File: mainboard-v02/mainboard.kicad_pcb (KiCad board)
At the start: 4 copper layers, 90.2 x 95.9 mm, 137 parts, among them J1 503182-1852, J2 Conn_01x05, J3 10118194-0001LF, J4 DCJ0303, J5 Conn_Coaxial, J6 Conn_Coaxial, J7 Conn_Coaxial, J8 Conn_01x03, Q1 IRLML2803, Q2 2N5088, Q3 2N5088, Q4 IRLML2803, Q5 IRLML2803, Q6 IRLML2803, Q7 IRLML2803, Q8 IRLML2803, SW1 KMR231NG LFS, U1 MAX708RESA-T, U10 XTB-40, U11 XTB-40, U12 XTB-40, U13 EP2W+, U14 S1216V8, U15 RFM23BP, U16 PE014006, U17 PE014006, U18 NDS8434, U19 NDS8434, U2 ATSAMD51J20A-AU, U20 NDS8434, U21 NDS8434, U22 NDS8434, U3 LSM9DS1, U4 MAX4372TEUK+T, U5 TPS54226PWPRPWP14_2P31X2P46-L, U6 LTC4121, U7 NDS8434, U8 MR25H40MDF, U9 XTB-40, Y1 32.768kHz

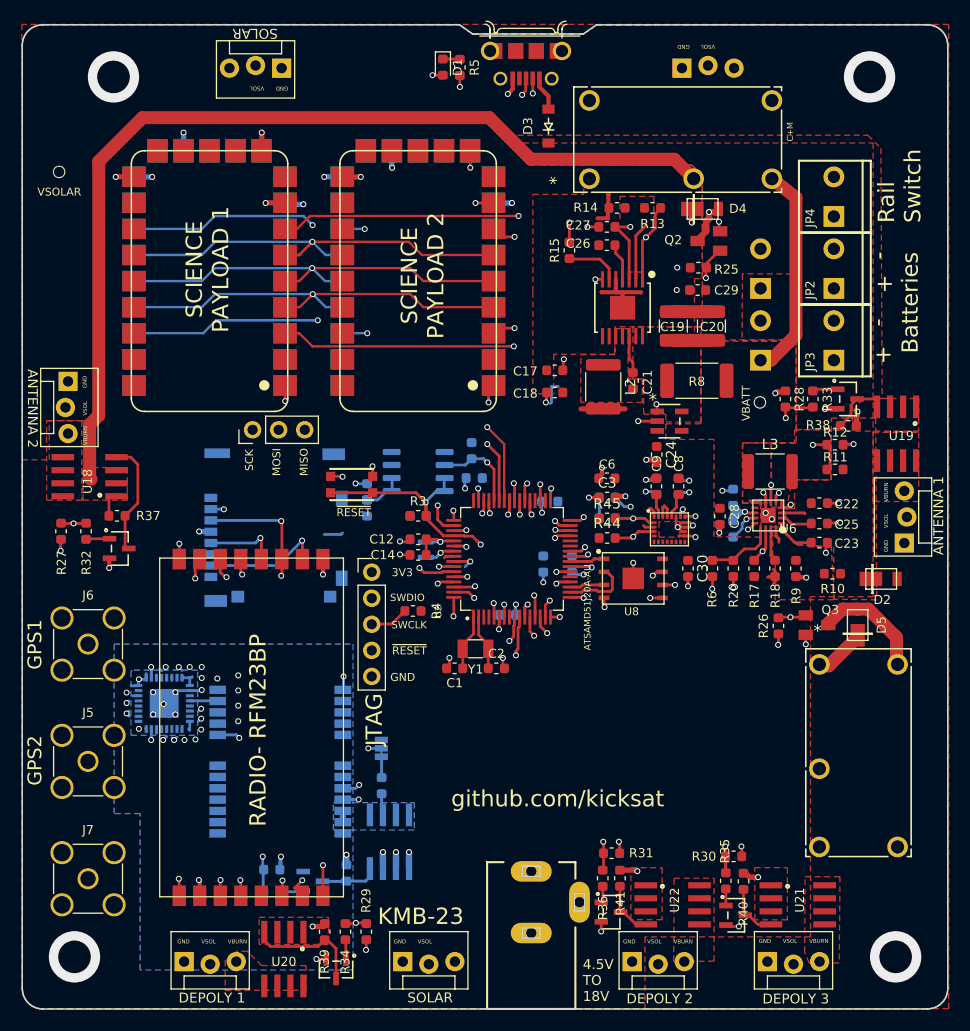
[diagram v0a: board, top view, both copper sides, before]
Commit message: mainboard-v02 with RFM98PW
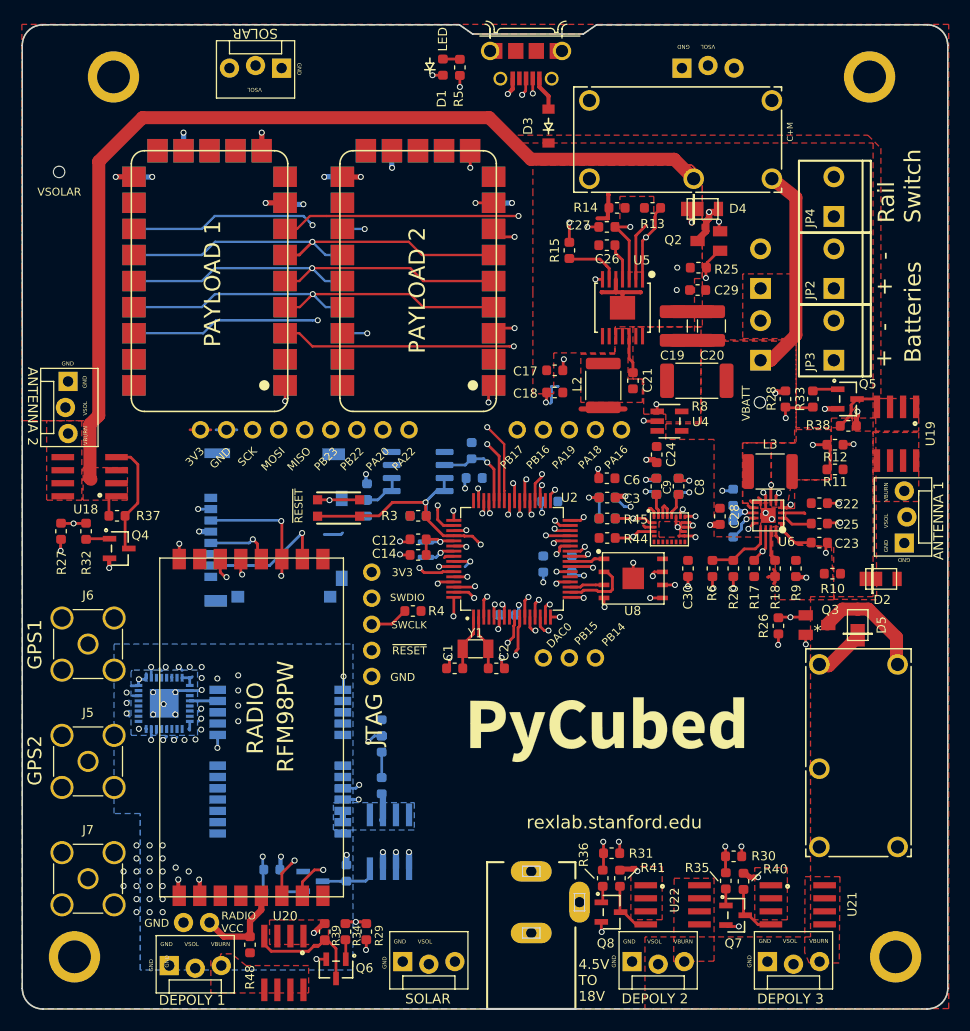
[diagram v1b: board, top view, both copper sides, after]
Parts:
- removed JP7: JUMPER-PAD-3-2OF3_NC_BY_TRACE_SMALL, mainboard:PAD-JUMPER-3-2OF3_NC_BY_TRACE_YES_SILK_FULL_BOX
- removed U15: RFM23BP, mainboard:RFM23BP
- added G***: LOGO, LOGO, B.Cu at (153.2, 120.4)
- added G***: LOGO, LOGO, F.Cu at (148.6, 127.1)
- added G***: LOGO, LOGO, F.Cu at (150.6, 123.7)
- added G***: LOGO, LOGO, B.Cu at (162.2, 127.1)
- added G*** (x2): LOGO, LOGO, F.Cu at (157.5, 120.4)
- added H1: MountingHole_Pad, MountingHole:MountingHole_3.2mm_M3_ISO7380_Pad, F.Cu at (107.2, 57.6)
- added H2: MountingHole_Pad, MountingHole:MountingHole_3.2mm_M3_DIN965_Pad, F.Cu at (103.4, 143.3)
- added H3: MountingHole_Pad, MountingHole:MountingHole_3.2mm_M3_DIN965_Pad, F.Cu at (183.4, 143.3)
- added H4: MountingHole_Pad, MountingHole:MountingHole_3.2mm_M3_DIN965_Pad, F.Cu at (180.9, 57.6)
- added J10: Conn_01x03, Connector_PinHeader_2.54mm:PinHeader_1x03_P2.54mm_Vertical, F.Cu at (149.1, 114.2)
- added J11: Conn_01x02, Connector_PinHeader_2.54mm:PinHeader_1x02_P2.54mm_Vertical, F.Cu at (116.6, 140.0)
- added J9: Conn_01x05, Connector_PinHeader_2.54mm:PinHeader_1x05_P2.54mm_Vertical, F.Cu at (146.6, 91.9)
- added R46: 0, Resistor_SMD:R_0603_1608Metric, B.Cu at (133.3, 121.0)
- added R47: 0, Resistor_SMD:R_0603_1608Metric, B.Cu at (133.3, 122.6)
- added R48: 0, Resistor_SMD:R_0603_1608Metric, F.Cu at (120.5, 142.1)
- added U23: RFM98PW, custom-footprints:RFM98PW, F.Cu at (121.1, 120.4)
- J8: value Conn_01x03 -> Conn_01x09; footprint Connector_PinHeader_2.54mm:PinHeader_1x03_P2.54mm_Vertical -> Connector_PinHeader_2.54mm:PinHeader_1x09_P2.54mm_Vertical
- U1: value MAX708RESA-T -> MAX706RS-T
- moved J8 5.08 mm to (115.7, 91.9)
- moved SW1 2.62 mm to (129.2, 99.6)
- moved JP13 1.51 mm to (112.6, 144.3)
- moved U20 0.38 mm to (123.8, 143.9)
- moved L2 0.13 mm to (154.9, 87.6)
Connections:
- net CS1 renamed PB17
- net CS2 renamed PB16
- net DRDY1 renamed PA18
- net DRDY2 renamed PA19
- J8 pad 1: SCK -> 3.3V
- J8 pad 2: MOSI -> GND
- J8 pad 3: MISO -> SCK
- U11 pad 3: CS4 -> PB22
- U11 pad 7: DRDY4 -> PA22
- U2 pad 27: Net-(U2-Pad27) -> PB14
- U2 pad 28: Net-(U2-Pad28) -> PB15
- U2 pad 35: BURN_RELAY_A -> PA16
- U2 pad 36: Net-(U2-Pad36) -> BURN_RELAY_A
- U2 pad 41: DRDY3 -> PA20
- U2 pad 43: DRDY4 -> PA22
- U2 pad 49: CS4 -> PB22
- U2 pad 50: CS3 -> PB23
- U2 pad 59: SPI_CS_RFM -> CS_RF
- U2 pad 6: ENAB_GPS -> RF_IO0
- U2 pad 61: RF_NIRQ -> RF_RST
- U2 pad 62: RF_SDN -> ENAB_GPS
- U2 pad 9: RF_IO2 -> RF_IO1
- U8 pad 3: Net-(U8-Pad3) -> FLASH_IO2
- U8 pad 7: Net-(U8-Pad7) -> FLASH_IO3
- U9 pad 3: CS3 -> PB23
- U9 pad 7: DRDY3 -> PA20
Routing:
- net PA20: track 0.00 -> 59.3 mm, vias 0 -> 2
- net DRDY3: track 58.2 -> 0.00 mm, vias 2 -> 0
- net PB23: track 0.00 -> 48.4 mm, vias 0 -> 2
- net CS3: track 44.5 -> 0.00 mm, vias 2 -> 0
- net RF_IO0: track 0.00 -> 40.1 mm, vias 0 -> 2
- net RF_IO1: track 0.00 -> 39.4 mm, vias 0 -> 2
- net RF_IO2: track 38.3 -> 0.00 mm, vias 2 -> 0
- net RF_SDN: track 38.0 -> 0.00 mm, vias 2 -> 0
- net PA22: track 0.00 -> 37.7 mm, vias 0 -> 2
- net DRDY4: track 34.1 -> 0.00 mm, vias 2 -> 0
- net PB22: track 0.00 -> 27.2 mm, vias 0 -> 2
- net RF_RST: track 0.00 -> 26.8 mm, vias 0 -> 2
- net RF_NIRQ: track 26.8 -> 0.00 mm, vias 2 -> 0
- net CS4: track 24.2 -> 0.00 mm, vias 2 -> 0
- net CS_RF: track 0.00 -> 23.4 mm, vias 0 -> 2
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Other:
- net class Default: via_dia 0.5842 -> 0.6; via_drill 0.381 -> 0.4
- rule pad_to_mask_clearance: 0.051 -> 0.0508
- rule trace_min: 0.127 -> 0.2
- board text added: "DAC0"
- board text added: "GPS"
- board text added: "GPS ~RST"
- board text added: "HOLLIDAY"
- board text added: "LED"
- board text added: "ON/OFF"
- board text added: "PA16"
- board text added: "PA18"
- board text added: "PA19"
- board text added: "PA20"
- board text added: "PA22"
- board text added: "PAYLOAD 1"
- board text added: "PAYLOAD 2"
- board text added: "PAYLOAD 3"
- board text added: "PAYLOAD 4"
- board text added: "PB14"
- board text added: "PB15"
- board text added: "PB16"
- board text added: "PB17"
- board text added: "PB22"
- board text added: "PB23"
- board text added: "RADIO VCC"
- board text added: "RFM98PW"
- board text added: "WDT"
- board text added: "rexlab.stanford.edu"
- board text removed: "GPS !RST"
- board text removed: "KMB-23"
- board text removed: "SCIENCE PAYLOAD 1"
- board text removed: "SCIENCE PAYLOAD 2"
- board text removed: "SENSOR 3"
- board text removed: "SENSOR 4"
- board text removed: "github.com/kicksat"
